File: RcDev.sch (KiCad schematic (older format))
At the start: 38 parts, among them J1 Thro CH4, J10 VBatt, J2 Ruddr CH3, J3 Program, J4 Elev CH2, J5 Aile CH1, J6 Model Power 7V4, J7 USB_B_Mini, J8 Batt1 3V7, J9 Batt2 3V7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

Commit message: Tweaks to make it more correct to assembly in 3D view (no real change to PCBs)
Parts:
- J3: footprint TrevM:PinHeader_1x06_P2.54mm_Vertical_bentR -> TrevM:PinHeader_1x06_P2.54mm_Vertical_bent
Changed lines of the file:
@@
 F 0 "J3" H 7772 1724 50  0000 R CNN
 F 1 "Program" H 7772 1633 50  0000 R CNN
-F 2 "TrevM:PinHeader_1x06_P2.54mm_Vertical_bentR" H 7800 1750 50  0001 C CNN
+F 2 "TrevM:PinHeader_1x06_P2.54mm_Vertical_bent" H 7800 1750 50  0001 C CNN
 F 3 "~" H 7800 1750 50  0001 C CNN
 	1    7800 1750

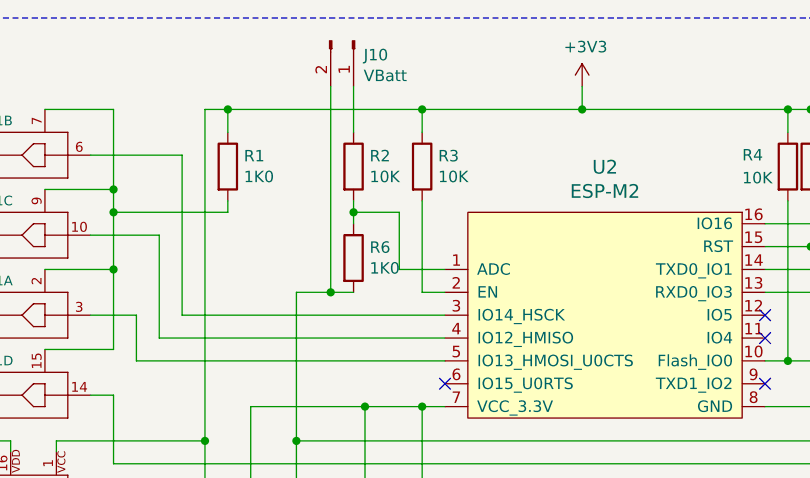
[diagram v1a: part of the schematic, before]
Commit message: Added 100nF capacitor to ADC
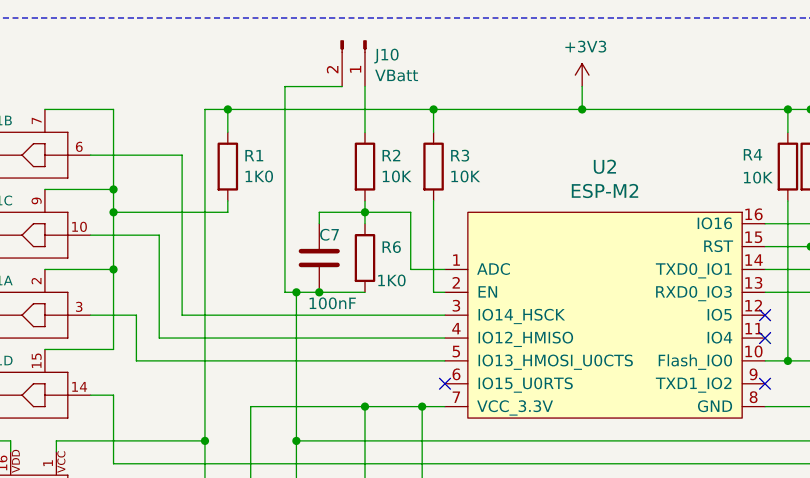
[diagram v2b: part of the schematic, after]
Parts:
- added C7: 100nF, Capacitor_SMD:C_0805_2012Metric, symbol Device:C
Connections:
- net GND: now also C7.2
- net at R2.2, R6.1, U2.1 (ADC): now also C7.1
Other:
- moved on the sheet: J10, R2, R3, R6
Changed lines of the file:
@@
 L Device:R R3
 U 1 1 60B64869
-P 5300 1300
-F 0 "R3" H 5370 1346 50  0000 L CNN
-F 1 "10K" H 5370 1255 50  0000 L CNN
-F 2 "Resistor_SMD:R_0805_2012Metric" V 5230 1300 50  0001 C CNN
-F 3 "~" H 5300 1300 50  0001 C CNN
-	1    5300 1300
-	1    0    0    -1
-$EndComp
-Wire Wire Line
-	5400 1850 5300 1850
-Wire Wire Line
-	5300 1850 5300 1450
-Wire Wire Line
-	5300 1150 5300 1050
+P 5350 1300
+F 0 "R3" H 5420 1346 50  0000 L CNN
+F 1 "10K" H 5420 1255 50  0000 L CNN
+F 2 "Resistor_SMD:R_0805_2012Metric" V 5280 1300 50  0001 C CNN
+F 3 "~" H 5350 1300 50  0001 C CNN
+	1    5350 1300
+	1    0    0    -1
+$EndComp
+Wire Wire Line
+	5400 1850 5350 1850
+Wire Wire Line
+	5350 1850 5350 1450
+Wire Wire Line
+	5350 1150 5350 1050
 Connection ~ 6900 1050
 Wire Wire Line
 	4550 2350 5050 2350
-Connection ~ 5300 1050
+Connection ~ 5350 1050
 $Comp
 L RcCtrl-eagle-import:CD40109BPW U1
@@
 	6000 950  6000 1050
 Wire Wire Line
-	5300 1050 6000 1050
+	5350 1050 6000 1050
 Connection ~ 6000 1050
 Wire Wire Line
@@
 Connection ~ 4450 1050
 Wire Wire Line
-	4450 1050 5300 1050
+	4450 1050 5350 1050
 Wire Wire Line
 	4450 1450 4450 1500
@@
 L Device:R R2
 U 1 1 611346A8
-P 5000 1300
-F 0 "R2" H 5070 1346 50  0000 L CNN
-F 1 "10K" H 5070 1255 50  0000 L CNN
-F 2 "Resistor_SMD:R_0805_2012Metric" V 4930 1300 50  0001 C CNN
-F 3 "~" H 5000 1300 50  0001 C CNN
-	1    5000 1300
+P 5050 1300
+F 0 "R2" H 5120 1346 50  0000 L CNN
+F 1 "10K" H 5120 1255 50  0000 L CNN
+F 2 "Resistor_SMD:R_0805_2012Metric" V 4980 1300 50  0001 C CNN
+F 3 "~" H 5050 1300 50  0001 C CNN
+	1    5050 1300
 	1    0    0    -1
 $EndComp
@@
 L Device:R R6
 U 1 1 6113556B
-P 5000 1700
-F 0 "R6" H 5070 1746 50  0000 L CNN
-F 1 "1K0" H 5070 1655 50  0000 L CNN
-F 2 "Resistor_SMD:R_0805_2012Metric" V 4930 1700 50  0001 C CNN
-F 3 "~" H 5000 1700 50  0001 C CNN
-	1    5000 1700
-	1    0    0    -1
-$EndComp
-Wire Wire Line
-	5000 950  5000 1150
-Wire Wire Line
-	5000 1450 5000 1500
-Wire Wire Line
-	5400 1750 5200 1750
-Wire Wire Line
-	5200 1750 5200 1500
-Wire Wire Line
-	5200 1500 5000 1500
-Connection ~ 5000 1500
-Wire Wire Line
-	5000 1500 5000 1550
+P 5050 1700
+F 0 "R6" H 5120 1746 50  0000 L CNN
+F 1 "1K0" H 5100 1600 50  0000 L CNN
+F 2 "Resistor_SMD:R_0805_2012Metric" V 4980 1700 50  0001 C CNN
+F 3 "~" H 5050 1700 50  0001 C CNN
+	1    5050 1700
+	1    0    0    -1
+$EndComp
+Wire Wire Line
+	5050 950  5050 1150
+Wire Wire Line
+	5050 1450 5050 1500
+Wire Wire Line
+	5400 1750 5250 1750
+Wire Wire Line
+	5250 1750 5250 1500
+Wire Wire Line
+	5250 1500 5050 1500
+Connection ~ 5050 1500
+Wire Wire Line
+	5050 1500 5050 1550
 Connection ~ 4750 2500
 Wire Wire Line
@@
 L conn:Conn_01x02_Male J10
 U 1 1 60C0DD9A
-P 5000 750
-F 0 "J10" V 5062 794 50  0000 L CNN
-F 1 "VBatt" V 5153 794 50  0000 L CNN
-F 2 "Connector_PinHeader_2.54mm:PinHeader_1x02_P2.54mm_Vertical" H 5000 750 50  0001 C CNN
-F 3 "~" H 5000 750 50  0001 C CNN
-	1    5000 750
+P 5050 750
+F 0 "J10" V 5112 794 50  0000 L CNN
+F 1 "VBatt" V 5203 794 50  0000 L CNN
+F 2 "Connector_PinHeader_2.54mm:PinHeader_1x02_P2.54mm_Vertical" H 5050 750 50  0001 C CNN
+F 3 "~" H 5050 750 50  0001 C CNN
+	1    5050 750
 	0    1    1    0
 $EndComp
@@
 Wire Wire Line
 	4750 2500 4750 1850
-Wire Wire Line
-	4750 1850 4900 1850
-Wire Wire Line
-	4900 950  4900 1850
-Connection ~ 4900 1850
-Wire Wire Line
-	4900 1850 5000 1850
 Text Label 3150 4150 0    50   ~ 0
 O+
 Text Label 3150 4250 0    50   ~ 0
 O-
+Connection ~ 4750 1850
+Wire Wire Line
+	4750 1850 4850 1850
+$Comp
+L Device:C C7
+U 1 1 60D11660
+P 4850 1700
+F 0 "C7" H 4850 1800 50  0000 L CNN
+F 1 "100nF" H 4800 1500 50  0000 L CNN
+F 2 "Capacitor_SMD:C_0805_2012Metric" H 4888 1550 50  0001 C CNN
+F 3 "~" H 4850 1700 50  0001 C CNN
+	1    4850 1700
+	1    0    0    -1
+$EndComp
+Wire Wire Line
+	4750 1850 4700 1850
+Wire Wire Line
+	4700 1850 4700 950
+Wire Wire Line
+	4700 950  4950 950
+Connection ~ 4850 1850
+Wire Wire Line
+	4850 1850 5050 1850
+Wire Wire Line
+	5050 1500 4850 1500
+Wire Wire Line
+	4850 1500 4850 1550
 $EndSCHEMATC
